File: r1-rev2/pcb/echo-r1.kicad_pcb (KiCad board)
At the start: 6 copper layers, 140 x 120.6 mm, 153 parts, among them J1 TYPE-C-31-M-12, J2 TF-115, J3 HP_3.5mm, J4 LO_3.5mm, J5 GT-BTP30003-xxxA-16A, J6 AFC07-S30ECA-00, J7 Conn_01x04, J8 Conn_01x05, J9 Micro_SD_Card, Q1 AO3401A, Q2 AO3401A, Q3 AO3401A, Q4 AO3401A, Q5 AO3401A, SW1 A, SW10 SELECT, SW11 VOL+, SW12 VOL-, SW13 POWER, SW14 HOLD, SW2 B, SW3 X, SW4 Y, SW5 DPAD↑, SW6 DPAD↓, SW7 DPAD←, SW8 DPAD→, SW9 START, U1 STM32H7R3Z8Jx, U10 USBLC6-2SC6, U11 TPAZ1143-04F, U12 TPAZ1143-04F, U13 TPAZ1143-04F, U14 TPAZ1143-04F, U15 TPAZ1143-04F, U16 TPAZ1143-04F, U2 W958D8NBYA5I, U3 TLV320AIC3104, U4 LM66100DCK, U5 TPS62A01DRLR, U6 TPS62A01DRLR, U7 AP2125K-3.0, U8 AP2125K-3.0, U9 TP4057, Y1 SC-32S32.768kHz20PPM12.5pF, Y2 XTM32024000JT00351001

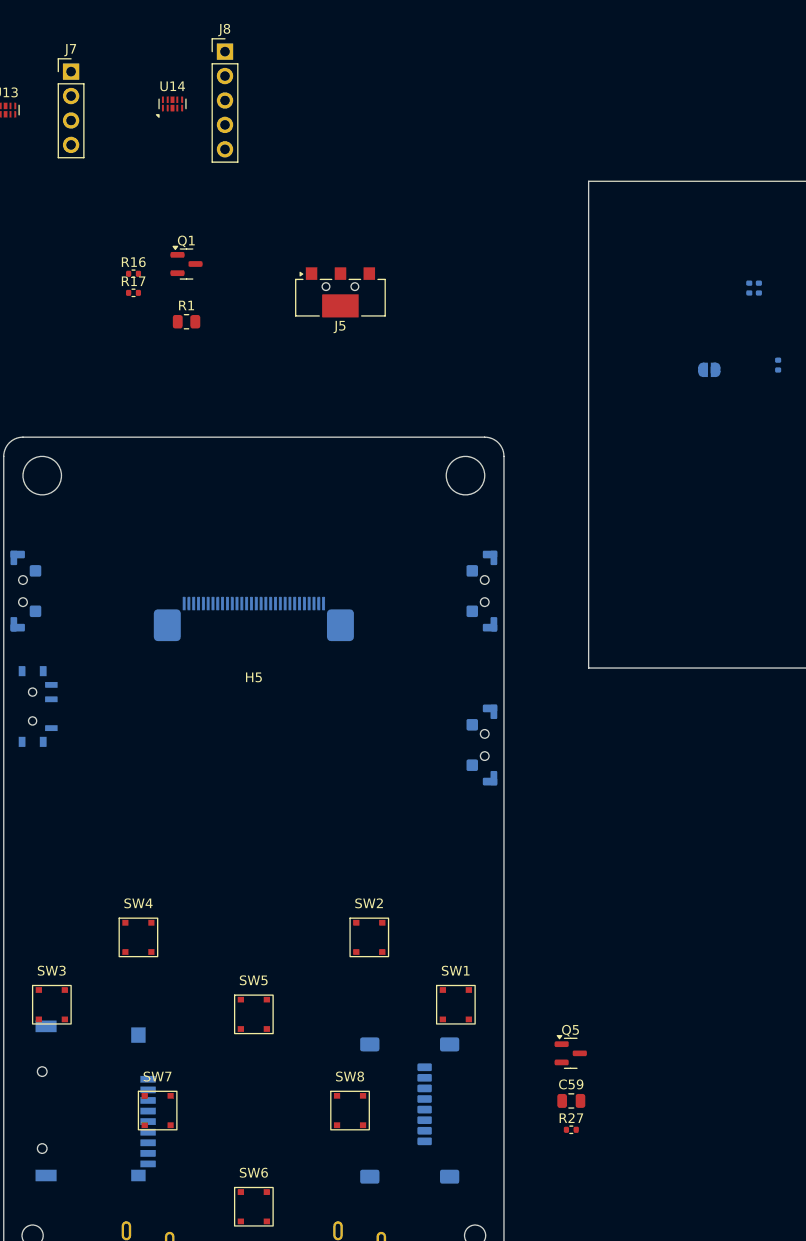
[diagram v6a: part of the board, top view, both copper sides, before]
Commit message: R1-Rev2: place battery connector and fix footprint courtyard
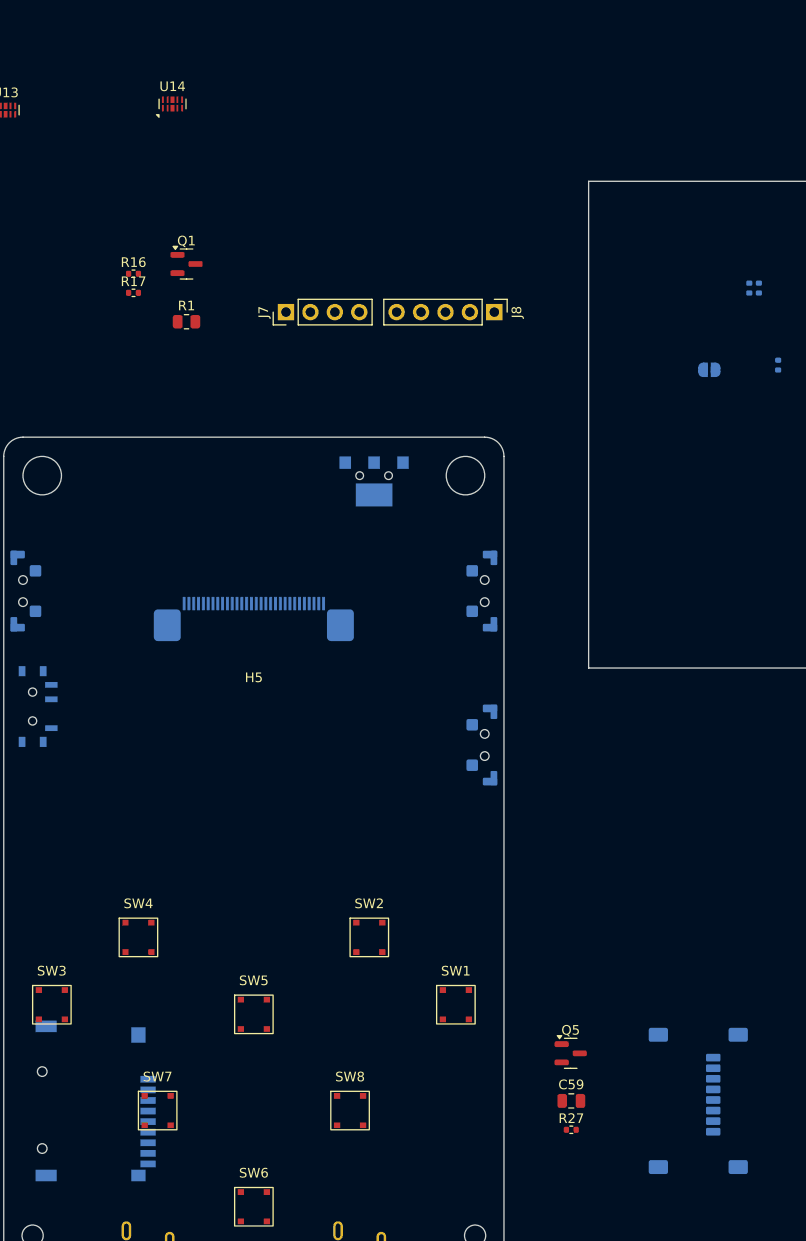
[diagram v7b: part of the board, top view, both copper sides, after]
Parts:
- J5: moved to B.Cu
- moved J8 39.0 mm to (172.5, 45.0), turned to -90 degrees
- moved J7 33.5 mm to (150.8, 45.0), turned to 90 degrees
- moved J9 30.0 mm to (192.5, 127.0)
- moved J5 20.0 mm to (160.0, 62.0), turned to 180 degrees
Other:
- board text added: "BATTERY"

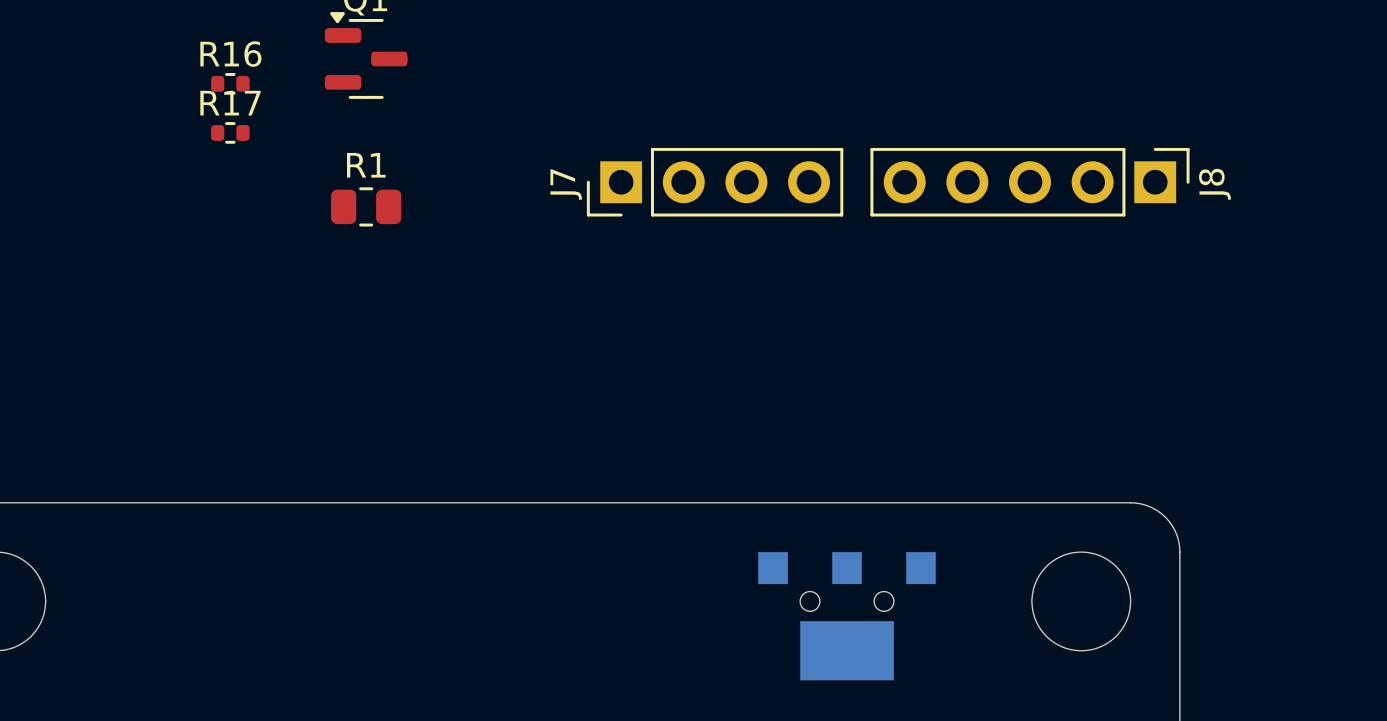
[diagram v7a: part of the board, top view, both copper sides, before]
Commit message: R1-Rev2: combine SWD/UART connectors into a single 1x7 header
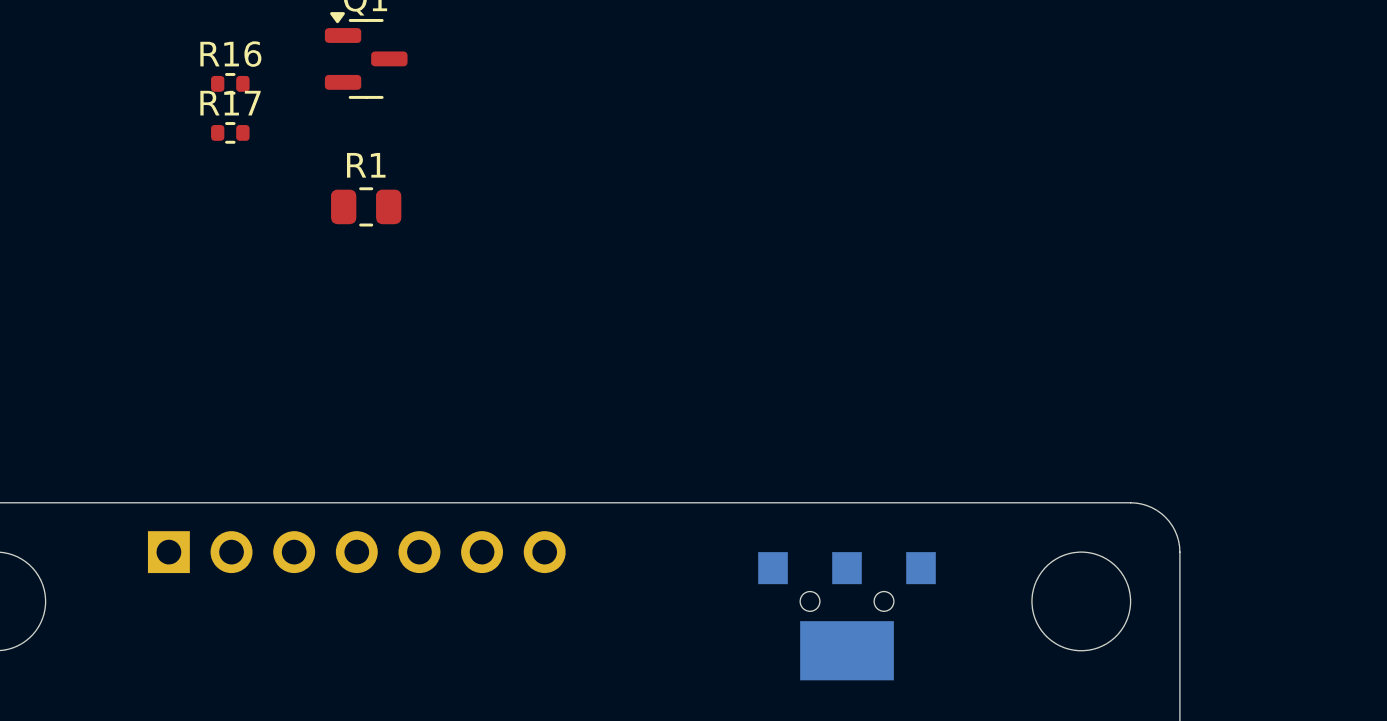
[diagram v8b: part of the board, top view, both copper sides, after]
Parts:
- removed J8: Conn_01x05, Connector_PinHeader_2.54mm:PinHeader_1x05_P2.54mm_Vertical
- J7: value Conn_01x04 -> Conn_SWDUART; footprint Connector_PinHeader_2.54mm:PinHeader_1x04_P2.54mm_Vertical -> Connector_PinHeader_2.54mm:PinHeader_1x07_P2.54mm_Vertical; moved to B.Cu
- moved J7 23.7 mm to (132.5, 60.0), turned to -90 degrees
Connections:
- J7 pad 1: /uart_tx -> /swd.nrst
- J7 pad 2: GND -> /swd.io
- J7 pad 3: /uart_rx -> GND
- J7 pad 4: +3V3 -> /swd.clk
- U13 pad 2: GND -> /uart_rx
- U13 pad 4: /uart_rx -> GND
- U13 pad 5: +3V3 -> GND
